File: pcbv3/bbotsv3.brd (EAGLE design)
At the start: 60 x 60 mm, 13 parts

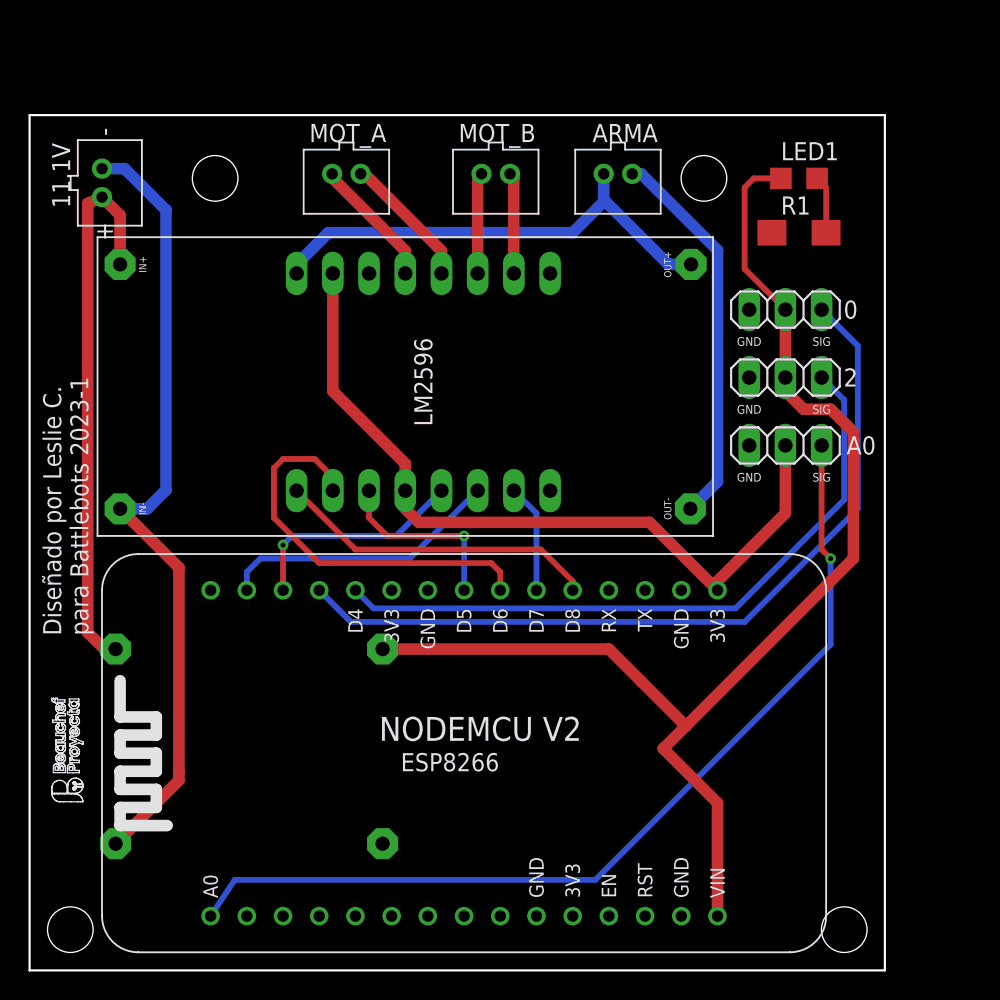
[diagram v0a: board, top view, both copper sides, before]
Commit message: added connections for voltage tester
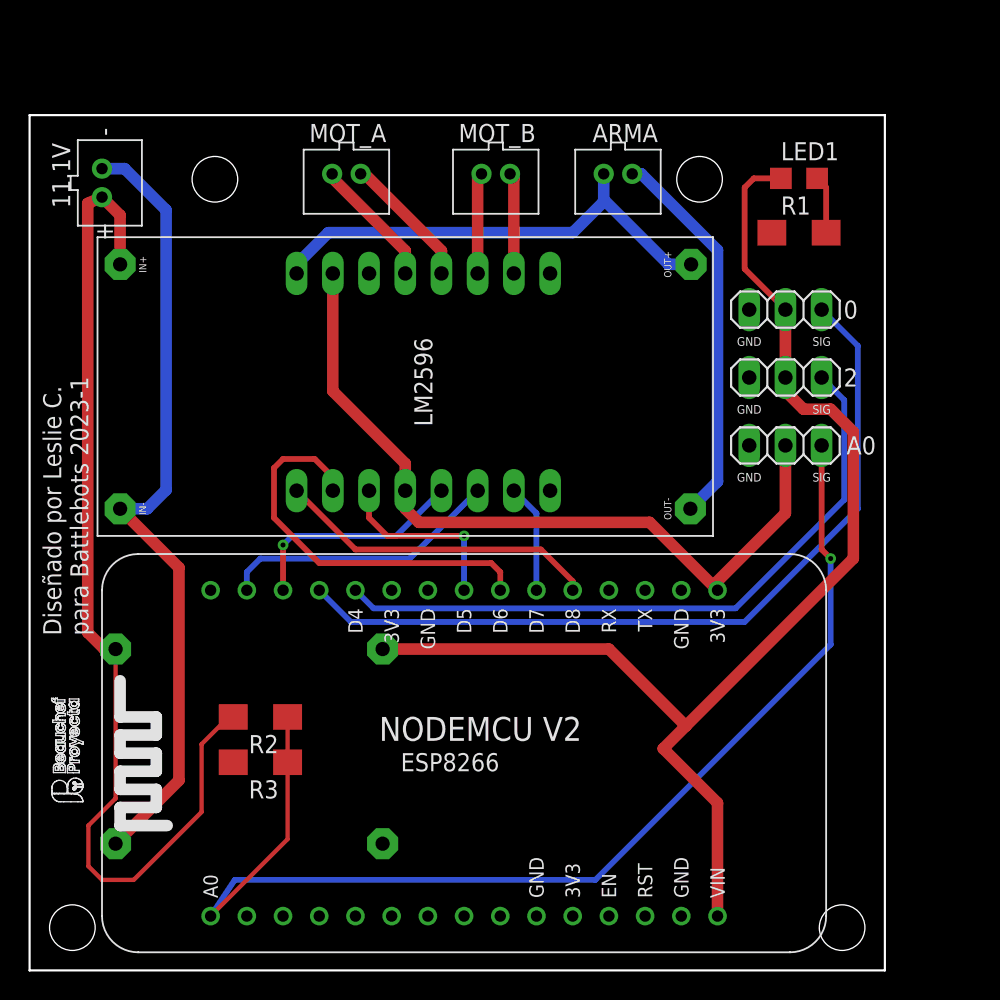
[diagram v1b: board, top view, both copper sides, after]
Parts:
- added R2, R3: BB-R1205, my-library:R1206
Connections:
- removed net N$21: A0.S, NODE1.A0
- new net N$1: A0.S, NODE1.A0, R2.1, R3.1
- net 11.1: now also R2.2
- net GND2: now also R3.2
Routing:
- net N$1: track 0.00 -> 82.1 mm, vias 0 -> 1
- net N$21: track 65.9 -> 0.00 mm, vias 1 -> 0
- net 11.1: track 38.9 -> 73.0 mm
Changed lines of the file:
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@@
 <drawing>
 <settings>
-<setting alwaysvectorfont="no"/>
+<setting alwaysvectorfont="yes"/>
 <setting verticaltext="up"/>
 </settings>
@@
 </layers>
 <board>
-<fusionsync huburn="a.cGVyc29uYWw6dWUyYzRkOTA5" projecturn="a.cGVyc29uYWw6dWUyYjkxNGFhIzIwMjIwNzIyNTQxNDA4NzAx" f3durn="urn:adsk.wipprod:dm.lineage:LMK6uCyRSQKW0e5iuERoUA" pcbguid="" lastpulledtime="2023-03-16T21:56:27Z" lastsyncedchangeguid="" latestrevisionid="9882951e-8a9e-4c36-89ad-65b980512b03" lastsyncedrevisionid="9882951e-8a9e-4c36-89ad-65b980512b03" lastboardhashguid="ad2a7377-8e42-527c-9697-7269814dbc61" lastpushedtime="2023-03-21T21:06:29Z" linktopcb3d="true"/>
+<fusionsync huburn="a.cGVyc29uYWw6dWUyYzRkOTA5" projecturn="a.cGVyc29uYWw6dWUyYjkxNGFhIzIwMjIwNzIyNTQxNDA4NzAx" f3durn="urn:adsk.wipprod:dm.lineage:LMK6uCyRSQKW0e5iuERoUA" pcbguid="" lastpulledtime="2023-03-27T01:48:59Z" lastsyncedchangeguid="" latestrevisionid="05a9330f-c07f-4a44-a290-e2be796a0c8a" lastsyncedrevisionid="05a9330f-c07f-4a44-a290-e2be796a0c8a" lastboardhashguid="1d4ad433-0ac7-83da-5812-4011d630a0d9" lastpushedtime="2023-03-27T01:52:02Z" linktopcb3d="true"/>
 <plain>
-<wire x1="0" y1="60" x2="0" y2="0" width="0.1524" layer="20"/>
-<wire x1="0" y1="0" x2="60" y2="0" width="0.1524" layer="20"/>
-<wire x1="60" y1="0" x2="60" y2="60" width="0.1524" layer="20"/>
-<wire x1="60" y1="60" x2="0" y2="60" width="0.1524" layer="20"/>
 <text x="4.1275" y="23.495" size="1.27" layer="21" rot="R90">Diseñado por Leslie C.
 para Battlebots 2023-1</text>
@@
 <wire x1="3.245" y1="13.0255" x2="3.245" y2="12.8941" width="0.0762" layer="21"/>
 <wire x1="3.245" y1="12.8941" x2="3.36875" y2="12.89081875" width="0.0762" layer="21"/>
-<hole x="13.0175" y="55.5625" drill="3.2"/>
-<hole x="2.8575" y="2.8575" drill="3.2"/>
-<hole x="57.15" y="2.8575" drill="3.2"/>
-<hole x="47.3075" y="55.5625" drill="3.2"/>
+<text x="54.61" y="6.6675" size="1.27" layer="22" rot="MR90">Diseñado por Leslie C.
+para Battlebots 2023-1</text>
+<hole x="13" y="55.5" drill="3.2"/>
+<hole x="3" y="3" drill="3.2"/>
+<hole x="57" y="3" drill="3.2"/>
+<hole x="47" y="55.5" drill="3.2"/>
+<wire x1="0" y1="60" x2="0" y2="0" width="0.1524" layer="20"/>
+<wire x1="0" y1="0" x2="60" y2="0" width="0.1524" layer="20"/>
+<wire x1="60" y1="0" x2="60" y2="60" width="0.1524" layer="20"/>
+<wire x1="60" y1="60" x2="0" y2="60" width="0.1524" layer="20"/>
 </plain>
 <attributes>
@@
 </element>
 <element name="U$3" library="my-library" library_urn="urn:adsk.eagle:library:37248401" package="LM2596MINIV2" package3d_urn="urn:adsk.eagle:package:39782154/1" value="BB-LM2596MINILM2596MINIV2" x="26.67" y="24.13" smashed="yes" rot="MR270"/>
+<element name="R2" library="my-library" library_urn="urn:adsk.eagle:library:37248401" package="R1206" package3d_urn="urn:adsk.eagle:package:39750174/1" value="BB-R1205" x="16.1925" y="17.78" smashed="yes" rot="R180">
+<attribute name="NAME" x="17.4625" y="16.50999375" size="1.27" layer="25" rot="R180"/>
+</element>
+<element name="R3" library="my-library" library_urn="urn:adsk.eagle:library:37248401" package="R1206" package3d_urn="urn:adsk.eagle:package:39750174/1" value="BB-R1205" x="16.1925" y="14.605" smashed="yes" rot="R180">
+<attribute name="NAME" x="17.4625" y="13.335" size="1.27" layer="25" rot="R180"/>
+</element>
 </elements>
 <signals>
@@
 <wire x1="4.08" y1="23.70125" x2="5.23875" y2="22.5425" width="0.8128" layer="1"/>
 <wire x1="5.23875" y1="22.5425" x2="6.0325" y2="22.5425" width="0.8128" layer="1"/>
+<contactref element="R2" pad="2"/>
+<wire x1="6.0325" y1="22.5425" x2="6.0325" y2="12.065" width="0.3048" layer="1"/>
+<wire x1="6.0325" y1="12.065" x2="4.1275" y2="10.16" width="0.3048" layer="1"/>
+<wire x1="4.1275" y1="10.16" x2="4.1275" y2="7.3025" width="0.3048" layer="1"/>
+<wire x1="4.1275" y1="7.3025" x2="5.08" y2="6.35" width="0.3048" layer="1"/>
+<wire x1="5.08" y1="6.35" x2="7.3025" y2="6.35" width="0.3048" layer="1"/>
+<wire x1="7.3025" y1="6.35" x2="12.065" y2="11.1125" width="0.3048" layer="1"/>
+<wire x1="12.065" y1="11.1125" x2="12.065" y2="15.875" width="0.3048" layer="1"/>
+<wire x1="12.065" y1="15.875" x2="13.97" y2="17.78" width="0.3048" layer="1"/>
+<wire x1="13.97" y1="17.78" x2="14.2875" y2="17.78" width="0.3048" layer="1"/>
 </signal>
 <signal name="5V">
@@
 <contactref element="0" pad="P"/>
 <contactref element="2" pad="P"/>
-<wire x1="42.8625" y1="20.32" x2="46.0375" y2="17.145" width="0.8128" layer="1"/>
+<wire x1="40.64" y1="22.5425" x2="46.0375" y2="17.145" width="0.8128" layer="1"/>
 <wire x1="44.45" y1="15.5575" x2="48.26" y2="11.7475" width="0.8128" layer="1"/>
 <wire x1="48.26" y1="11.7475" x2="48.26" y2="3.81" width="0.8128" layer="1"/>
@@
 <contactref element="U$3" pad="OUT+"/>
 <wire x1="24.765" y1="22.5425" x2="40.64" y2="22.5425" width="0.8128" layer="1"/>
-<wire x1="40.64" y1="22.5425" x2="42.8625" y2="20.32" width="0.8128" layer="1"/>
 </signal>
 <signal name="GND2">
@@
 <wire x1="46.355" y1="32.385" x2="48.26" y2="34.29" width="0.8128" layer="16"/>
 <wire x1="6.35" y1="32.385" x2="10.4775" y2="28.2575" width="0.8128" layer="1"/>
-<wire x1="10.4775" y1="28.2575" x2="10.4775" y2="13.97" width="0.8128" layer="1"/>
+<wire x1="10.4775" y1="28.2575" x2="10.4775" y2="13.335" width="0.8128" layer="1"/>
 <wire x1="5.08" y1="56.245" x2="6.6675" y2="56.245" width="0.8128" layer="16"/>
 <wire x1="9.5725" y1="53.34" x2="6.6675" y2="56.245" width="0.8128" layer="16"/>
@@
 <contactref element="U$3" pad="IN-"/>
 <contactref element="U$3" pad="OUT-"/>
-<wire x1="10.4775" y1="13.97" x2="10.4775" y2="13.335" width="0.8128" layer="1"/>
 <wire x1="10.4775" y1="13.335" x2="6.0325" y2="8.89" width="0.8128" layer="1"/>
+<contactref element="R3" pad="2"/>
 <wire x1="50.4825" y1="46.355" x2="52.07" y2="51.7525" width="0" layer="19" extent="1-1"/>
 <wire x1="50.4825" y1="41.5925" x2="50.4825" y2="46.355" width="0" layer="19" extent="1-1"/>
@@
 <wire x1="27.94" y1="26.67" x2="36.5125" y2="33.655" width="0" layer="19" extent="1-1"/>
 <wire x1="24.765" y1="8.89" x2="27.94" y2="26.67" width="0" layer="19" extent="1-1"/>
+<wire x1="14.2875" y1="14.605" x2="24.765" y2="8.89" width="0" layer="19" extent="1-1"/>
+<wire x1="6.0325" y1="8.89" x2="14.2875" y2="14.605" width="0" layer="19" extent="1-1"/>
 <wire x1="35.56" y1="3.81" x2="24.765" y2="8.89" width="0" layer="19" extent="1-1"/>
 <wire x1="45.72" y1="3.81" x2="35.56" y2="3.81" width="0" layer="19" extent="1-1"/>
-<wire x1="6.0325" y1="8.89" x2="24.765" y2="8.89" width="0" layer="19" extent="1-1"/>
 <wire x1="23.8125" y1="48.895" x2="42.275" y2="55.88" width="0" layer="19" extent="1-1"/>
 </signal>
@@
 <wire x1="21.225" y1="55.88" x2="21.2725" y2="55.8325" width="0.8128" layer="1"/>
 <wire x1="21.2725" y1="55.8325" x2="21.2725" y2="55.5625" width="0.8128" layer="1"/>
-</signal>
-<signal name="N$21">
-<contactref element="NODE1" pad="A0"/>
-<contactref element="A0" pad="S"/>
-<wire x1="12.7" y1="3.81" x2="14.393334375" y2="6.35" width="0.4064" layer="16"/>
-<wire x1="14.393334375" y1="6.35" x2="39.6875" y2="6.35" width="0.4064" layer="16"/>
-<wire x1="39.6875" y1="6.35" x2="56.1975" y2="22.86" width="0.4064" layer="16"/>
-<via x="56.1975" y="28.8925" extent="1-16" drill="0.35"/>
-<wire x1="56.1975" y1="28.8925" x2="55.5625" y2="29.5275" width="0.4064" layer="1"/>
-<wire x1="55.5625" y1="29.5275" x2="55.5625" y2="36.83" width="0.4064" layer="1"/>
-<wire x1="56.1975" y1="22.86" x2="56.1975" y2="28.8925" width="0.4064" layer="16"/>
 </signal>
 <signal name="N$4">
@@
 <wire x1="55.88" y1="54.9275" x2="55.88" y2="51.7525" width="0.4064" layer="1"/>
 </signal>
+<signal name="N$1">
+<contactref element="R2" pad="1"/>
+<contactref element="R3" pad="1"/>
+<contactref element="NODE1" pad="A0"/>
+<contactref element="A0" pad="S"/>
+<wire x1="12.7" y1="3.81" x2="14.393334375" y2="6.35" width="0.4064" layer="16"/>
+<wire x1="14.393334375" y1="6.35" x2="39.6875" y2="6.35" width="0.4064" layer="16"/>
+<wire x1="39.6875" y1="6.35" x2="56.1975" y2="22.86" width="0.4064" layer="16"/>
+<via x="56.1975" y="28.8925" extent="1-16" drill="0.35"/>
+<wire x1="56.1975" y1="28.8925" x2="55.5625" y2="29.5275" width="0.4064" layer="1"/>
+<wire x1="55.5625" y1="29.5275" x2="55.5625" y2="36.83" width="0.4064" layer="1"/>
+<wire x1="56.1975" y1="22.86" x2="56.1975" y2="28.8925" width="0.4064" layer="16"/>
+<wire x1="18.0975" y1="17.78" x2="18.0975" y2="14.605" width="0.3048" layer="1"/>
+<wire x1="18.0975" y1="14.605" x2="18.0975" y2="9.2075" width="0.3048" layer="1"/>
+<wire x1="18.0975" y1="9.2075" x2="12.7" y2="3.81" width="0.3048" layer="1"/>
+</signal>
 </signals>

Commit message: finish pcb, waiting review
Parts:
- removed 11.1V: (no value), adafruit:JST-PH-2-THM
- removed A0: 3.3, my-library:1X03
- removed LED1: (no value), my-library:R0805
- removed MOT_A, MOT_B: (no value), my-library:JST_2PIN
- added 5VREG: (no value), my-library:R0805
- added ARMA1, ARMA2, ARMA3: TERMINAL_2P, KF301-2P-Terminal:KF301-2P
- added D1: (no value), adafruit:DO-1N4148
- added E1: MSTBA2, con-phoenix-508:MSTBA2
- added Q1, Q2: (no value), adafruit:SOT23-W
- added R4, R5, R6, R7: 10k, my-library:R1206
- ARMA: value (none) -> TERMINAL_2P; device my-library:JST_2PIN -> KF301-2P-Terminal:KF301-2P
- R1: value BB-R1205 -> 100
- R2: value BB-R1205 -> 10k
- R3: value BB-R1205 -> 1k
- moved ARMA 13.9 mm to (54.9, 58.4), turned to 0 degrees
- moved R1 8.08 mm to (59.7, 46.0)
- moved 2 8.01 mm to (57.5, 34.9)
- moved 0 8.01 mm to (57.5, 39.7)
- moved U$1 4.86 mm to (9.53, 52.4)
- moved U$2 4.86 mm to (32.4, 42.2)
- moved U$3 3.62 mm to (30.2, 25.1)
- moved R2 3.31 mm to (19.4, 18.7)
- moved R3 3.31 mm to (19.4, 15.6)
- moved NODE1 3.31 mm to (32.4, 16.2)
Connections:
- removed net N$16: MOT_B.2, U$2.BO1
- new net N$11: 2.S, Q1.3, R6.1
- new net N$19: NODE1.D4, Q1.2, R5.1
- new net N$2: ARMA3.1, D1.A, E1.1
- net 11.1: now also D1.C; no longer 11.1V.1
- net 3V3: now also NODE1.3V3@1, NODE1.3V3@3, Q1.1, Q2.1, R4.2, R5.2, U$2.STBY, U$2.VCC
- net 5V: now also 5VREG.1, R6.2, R7.2; no longer LED1.1
- net GND2: now also ARMA3.2, E1.2, U$2.GND2; no longer 11.1V.2, A0.GND
- net N$1: no longer A0.S
- net N$12: now also NODE1.D3, Q2.2, R4.1; no longer 2.S, NODE1.D4
- net N$13: now also ARMA1.2; no longer MOT_A.2
- net N$14: now also ARMA1.1; no longer MOT_A.1
- net N$15: now also ARMA2.2, U$2.BO1; no longer MOT_B.1, U$2.BO2
- net N$18: now also Q2.3, R7.1; no longer NODE1.D3
- net N$3: now also 5VREG.2; no longer LED1.2
- net N$6: now also ARMA2.1, U$2.BO2; no longer A0.P, NODE1.3V3@1, NODE1.3V3@3, U$2.STBY, U$2.VCC
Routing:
- net 3V3: track 0.00 -> 69.2 mm
- net N$1: track 82.1 -> 16.2 mm, vias 1 -> 0
- net GND2: track 83.3 -> 26.3 mm
- net N$6: track 55.0 -> 11.0 mm
- net N$2: track 0.00 -> 23.7 mm
- net N$11: track 0.00 -> 23.0 mm, vias 0 -> 1
- net N$19: track 0.00 -> 22.2 mm
- net N$18: track 57.0 -> 37.6 mm, vias 0 -> 1
- net N$12: track 47.2 -> 29.2 mm
- net 11.1: track 73.0 -> 65.8 mm
- net N$16: track 7.10 -> 0.00 mm
- net N$15: track 7.10 -> 13.3 mm
- net 5V: track 88.8 -> 92.8 mm
- net 12V: track 34.0 -> 37.3 mm
- net N$9: track 15.9 -> 17.5 mm
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- added copper zone on layer 1, net GND2
- added copper zone on layer 16, net GND2
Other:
- board size 60 x 60 mm -> 66 x 66 mm
- board text added: "+"
- board text added: "-"
- board text added: "5V"
- board text added: "ARMA"
- board text added: "Diseño por Leslie C. para Battlebots 2023-1"
- board text added: "E2"
- board text added: "GND"
- board text added: "MOT_A"
- board text added: "MOT_B"
- board text removed: "Diseñado por Leslie C. para Battlebots 2023-1"
